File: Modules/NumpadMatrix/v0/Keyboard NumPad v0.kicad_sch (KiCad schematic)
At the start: 43 parts, among them U1 ESP32-C3_SUPERMINI

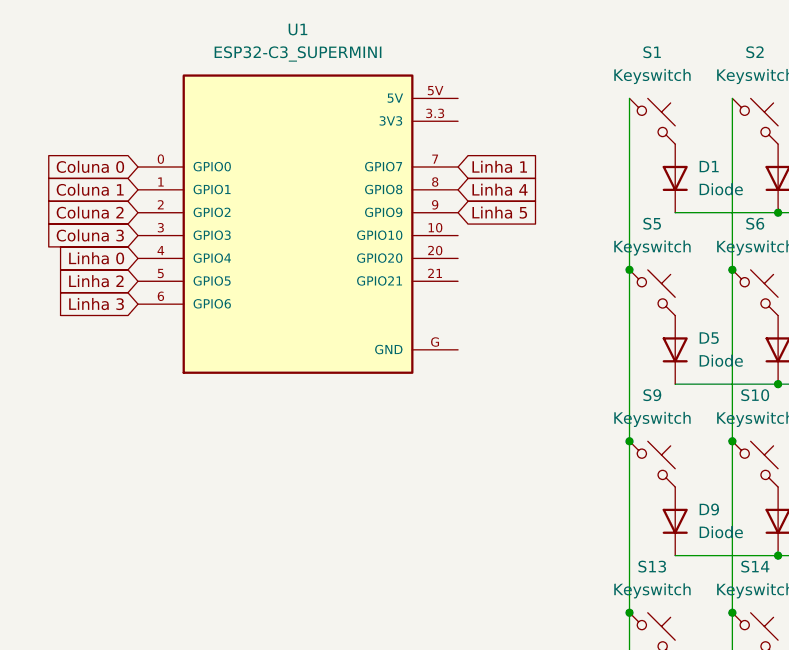
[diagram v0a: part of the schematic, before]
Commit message: iniciated the ControlerBoard V0. I need the screen size!!
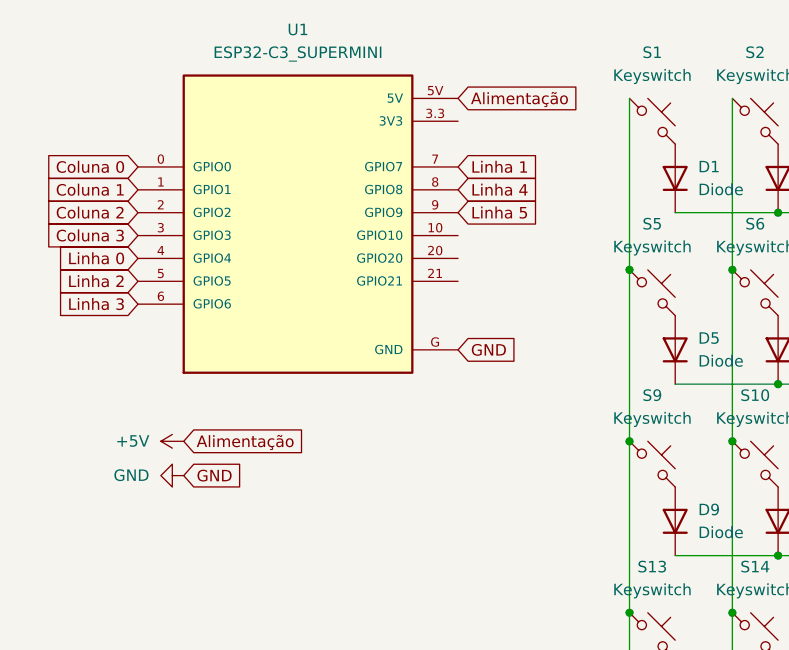
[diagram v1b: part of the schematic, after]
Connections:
- net +5V: now reaches U1.5V
- net GND: now reaches U1.G (GND)
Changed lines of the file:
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@@
 		)
 	)
+	(global_label "GND"
+		(shape input)
+		(at 85.09 64.77 0)
+		(fields_autoplaced yes)
+		(effects
+			(font
+				(size 1.27 1.27)
+			)
+			(justify left)
+		)
+		(property "Intersheetrefs" "${INTERSHEET_REFS}"
+			(at 91.9457 64.77 0)
+			(effects
+				(font
+					(size 1.27 1.27)
+				)
+				(justify left)
+				(hide yes)
+			)
+		)
+	)
 	(global_label "Coluna 3"
 		(shape input)
@@
 		)
 	)
+	(global_label "Alimentação"
+		(shape input)
+		(at 85.09 36.83 0)
+		(fields_autoplaced yes)
+		(effects
+			(font
+				(size 1.27 1.27)
+			)
+			(justify left)
+		)
+		(property "Intersheetrefs" "${INTERSHEET_REFS}"
+			(at 99.626 36.83 0)
+			(effects
+				(font
+					(size 1.27 1.27)
+				)
+				(justify left)
+				(hide yes)
+			)
+		)
+	)
+	(global_label "GND"
+		(shape input)
+		(at 54.61 78.74 0)
+		(fields_autoplaced yes)
+		(effects
+			(font
+				(size 1.27 1.27)
+			)
+			(justify left)
+		)
+		(property "Intersheetrefs" "${INTERSHEET_REFS}"
+			(at 61.4657 78.74 0)
+			(effects
+				(font
+					(size 1.27 1.27)
+				)
+				(justify left)
+				(hide yes)
+			)
+		)
+	)
 	(global_label "Linha 3"
 		(shape input)
@@
 		)
 	)
+	(global_label "Alimentação"
+		(shape input)
+		(at 54.61 74.93 0)
+		(fields_autoplaced yes)
+		(effects
+			(font
+				(size 1.27 1.27)
+			)
+			(justify left)
+		)
+		(property "Intersheetrefs" "${INTERSHEET_REFS}"
+			(at 69.146 74.93 0)
+			(effects
+				(font
+					(size 1.27 1.27)
+				)
+				(justify left)
+				(hide yes)
+			)
+		)
+	)
 	(global_label "Linha 1"
 		(shape input)
@@
 	)
 	(symbol
+		(lib_id "power:+5V")
+		(at 54.61 74.93 90)
+		(unit 1)
+		(exclude_from_sim no)
+		(in_bom yes)
+		(on_board yes)
+		(dnp no)
+		(fields_autoplaced yes)
+		(property "Reference" "#PWR01"
+			(at 58.42 74.93 0)
+			(effects
+				(font
+					(size 1.27 1.27)
+				)
+				(hide yes)
+			)
+		)
+		(property "Value" "+5V"
+			(at 50.8 74.9299 90)
+			(effects
+				(font
+					(size 1.27 1.27)
+				)
+				(justify left)
+			)
+		)
+		(property "Footprint" ""
+			(at 54.61 74.93 0)
+			(effects
+				(font
+					(size 1.27 1.27)
+				)
+				(hide yes)
+			)
+		)
+		(property "Datasheet" ""
+			(at 54.61 74.93 0)
+			(effects
+				(font
+					(size 1.27 1.27)
+				)
+				(hide yes)
+			)
+		)
+		(property "Description" "Power symbol creates a global label with name \"+5V\""
+			(at 54.61 74.93 0)
+			(effects
+				(font
+					(size 1.27 1.27)
+				)
+				(hide yes)
+			)
+		)
+		(pin "1"
+		)
+		(instances
+			(project ""
+				(path "/72d6a7bc-74bb-4585-b459-4dd0fcbeadc8"
+					(reference "#PWR01")
+					(unit 1)
+				)
+			)
+		)
+	)
+	(symbol
 		(lib_id "ScottoKeebs:Placeholder_Diode")
 		(at 109.22 121.92 90)
@@
 					(unit 1)
 				)
+			)
+		)
+	)
+	(symbol
+		(lib_id "power:GND")
+		(at 54.61 78.74 270)
+		(unit 1)
+		(exclude_from_sim no)
+		(in_bom yes)
+		(on_board yes)
+		(dnp no)
+		(fields_autoplaced yes)
+		(property "Reference" "#PWR02"
+			(at 48.26 78.74 0)
+			(effects
+				(font
+					(size 1.27 1.27)
+				)
+				(hide yes)
+			)
+		)
+		(property "Value" "GND"
+			(at 50.8 78.7399 90)
+			(effects
+				(font
+					(size 1.27 1.27)
+				)
+				(justify right)
+			)
+		)
+		(property "Footprint" ""
+			(at 54.61 78.74 0)
+			(effects
+				(font
+					(size 1.27 1.27)
+				)
+				(hide yes)
+			)
+		)
+		(property "Datasheet" ""
+			(at 54.61 78.74 0)
+			(effects
+				(font
+					(size 1.27 1.27)
+				)
+				(hide yes)
+			)
+		)
+		(property "Description" "Power symbol creates a global label with name \"GND\" , ground"
+			(at 54.61 78.74 0)
+			(effects
+				(font
+					(size 1.27 1.27)
+				)
+				(hide yes)
+			)
+		)
+		(pin "1"
+		)
+		(instances
+			(project ""
+				(path "/72d6a7bc-74bb-4585-b459-4dd0fcbeadc8"
+					(reference "#PWR02")
+					(unit 1)
+				)
